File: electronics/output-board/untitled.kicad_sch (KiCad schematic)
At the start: 5 parts, among them J17 Conn_01x02_Male

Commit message: Started updating the output board
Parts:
- added D?: 1N4007, Diode_THT:D_DO-41_SOD81_P10.16mm_Horizontal, symbol Diode:1N4007
- renumbered D13 to D9, J17 to J12, MOSFET13 to MOSFET8, R30 to R10, R29 to R23
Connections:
- net +12V: now also D?.1 (K)
- net at D9.1 (K), J12.1 (Pin_1), MOSFET8.3: now also D?.2 (A)
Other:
- moved on the sheet: D9, J12, MOSFET8, R10, R23
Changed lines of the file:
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@@
 (kicad_sch (version 20211123) (generator eeschema)
   (paper "A4")
-  (junction (at 49.53 36.83) (diameter 0) (color 0 0 0 0)
+  (junction (at 49.53 43.18) (diameter 0) (color 0 0 0 0)
   )
-  (junction (at 46.99 30.48) (diameter 0) (color 0 0 0 0)
+  (junction (at 44.45 30.48) (diameter 0) (color 0 0 0 0)
   )
-  (wire (pts (xy 62.23 36.83) (xy 67.31 36.83))
+  (junction (at 46.99 36.83) (diameter 0) (color 0 0 0 0)
+  )
+  (junction (at 52.07 30.48) (diameter 0) (color 0 0 0 0)
+  )
+  (wire (pts (xy 62.23 43.18) (xy 67.31 43.18))
     (stroke (width 0) (type default) (color 0 0 0 0))
   )
-  (wire (pts (xy 46.99 30.48) (xy 58.42 30.48))
+  (wire (pts (xy 46.99 35.56) (xy 44.45 35.56))
     (stroke (width 0) (type default) (color 0 0 0 0))
   )
-  (wire (pts (xy 49.53 54.61) (xy 49.53 57.15))
+  (wire (pts (xy 49.53 35.56) (xy 52.07 35.56))
     (stroke (width 0) (type default) (color 0 0 0 0))
   )
-  (wire (pts (xy 49.53 36.83) (xy 54.61 36.83))
+  (wire (pts (xy 46.99 36.83) (xy 58.42 36.83))
     (stroke (width 0) (type default) (color 0 0 0 0))
   )
-  (wire (pts (xy 66.04 30.48) (xy 67.31 30.48))
+  (wire (pts (xy 52.07 22.86) (xy 52.07 30.48))
     (stroke (width 0) (type default) (color 0 0 0 0))
   )
-  (wire (pts (xy 67.31 30.48) (xy 67.31 36.83))
+  (wire (pts (xy 49.53 60.96) (xy 49.53 63.5))
     (stroke (width 0) (type default) (color 0 0 0 0))
   )
-  (wire (pts (xy 24.13 57.15) (xy 49.53 57.15))
+  (wire (pts (xy 49.53 43.18) (xy 54.61 43.18))
     (stroke (width 0) (type default) (color 0 0 0 0))
   )
-  (wire (pts (xy 49.53 29.21) (xy 49.53 36.83))
+  (wire (pts (xy 66.04 36.83) (xy 67.31 36.83))
     (stroke (width 0) (type default) (color 0 0 0 0))
   )
-  (wire (pts (xy 49.53 36.83) (xy 49.53 39.37))
+  (wire (pts (xy 67.31 36.83) (xy 67.31 43.18))
     (stroke (width 0) (type default) (color 0 0 0 0))
   )
-  (wire (pts (xy 34.29 46.99) (xy 39.37 46.99))
+  (wire (pts (xy 24.13 63.5) (xy 49.53 63.5))
     (stroke (width 0) (type default) (color 0 0 0 0))
   )
-  (wire (pts (xy 24.13 46.99) (xy 26.67 46.99))
+  (wire (pts (xy 49.53 35.56) (xy 49.53 43.18))
     (stroke (width 0) (type default) (color 0 0 0 0))
   )
-  (wire (pts (xy 46.99 29.21) (xy 46.99 30.48))
+  (wire (pts (xy 49.53 43.18) (xy 49.53 45.72))
     (stroke (width 0) (type default) (color 0 0 0 0))
   )
-  (wire (pts (xy 45.72 30.48) (xy 46.99 30.48))
+  (wire (pts (xy 52.07 35.56) (xy 52.07 30.48))
     (stroke (width 0) (type default) (color 0 0 0 0))
   )
-  (wire (pts (xy 45.72 33.02) (xy 45.72 30.48))
+  (wire (pts (xy 44.45 30.48) (xy 44.45 22.86))
     (stroke (width 0) (type default) (color 0 0 0 0))
   )
-  (hierarchical_label "GROUND" (shape input) (at 24.13 57.15 180)
+  (wire (pts (xy 44.45 35.56) (xy 44.45 30.48))
+    (stroke (width 0) (type default) (color 0 0 0 0))
+  )
+  (wire (pts (xy 34.29 53.34) (xy 39.37 53.34))
+    (stroke (width 0) (type default) (color 0 0 0 0))
+  )
+  (wire (pts (xy 24.13 53.34) (xy 26.67 53.34))
+    (stroke (width 0) (type default) (color 0 0 0 0))
+  )
+  (wire (pts (xy 46.99 35.56) (xy 46.99 36.83))
+    (stroke (width 0) (type default) (color 0 0 0 0))
+  )
+  (wire (pts (xy 45.72 36.83) (xy 46.99 36.83))
+    (stroke (width 0) (type default) (color 0 0 0 0))
+  )
+  (wire (pts (xy 45.72 39.37) (xy 45.72 36.83))
+    (stroke (width 0) (type default) (color 0 0 0 0))
+  )
+  (wire (pts (xy 44.45 22.86) (xy 46.99 22.86))
+    (stroke (width 0) (type default) (color 0 0 0 0))
+  )
+  (wire (pts (xy 49.53 22.86) (xy 52.07 22.86))
+    (stroke (width 0) (type default) (color 0 0 0 0))
+  )
+  (hierarchical_label "GROUND" (shape input) (at 24.13 63.5 180)
     (effects (font (size 1.27 1.27)) (justify right))
   )
-  (hierarchical_label "INPUT" (shape input) (at 24.13 46.99 180)
+  (hierarchical_label "INPUT" (shape input) (at 24.13 53.34 180)
     (effects (font (size 1.27 1.27)) (justify right))
   )
-  (symbol (lib_id "power:+12V") (at 45.72 33.02 180)
+  (symbol (lib_id "power:+12V") (at 45.72 39.37 180)
     (in_bom yes) (on_board yes) (fields_autoplaced)
-    (property "Reference" "#PWR0144" (id 0) (at 45.72 29.21 0)
+    (property "Reference" "#PWR0140" (id 0) (at 45.72 35.56 0)
       (effects (font (size 1.27 1.27)) hide)
     )
-    (property "Value" "+12V" (id 1) (at 45.72 37.5826 0))
-    (property "Footprint" "" (id 2) (at 45.72 33.02 0)
+    (property "Value" "+12V" (id 1) (at 45.72 43.9326 0))
+    (property "Footprint" "" (id 2) (at 45.72 39.37 0)
       (effects (font (size 1.27 1.27)) hide)
     )
-    (property "Datasheet" "" (id 3) (at 45.72 33.02 0)
+    (property "Datasheet" "" (id 3) (at 45.72 39.37 0)
       (effects (font (size 1.27 1.27)) hide)
     )
     (pin "1")
   )
-  (symbol (lib_id "2021-09-18_15-04-13:BSS806NEH6327XTSA1") (at 39.37 46.99 0)
+  (symbol (lib_id "2021-09-18_15-04-13:BSS806NEH6327XTSA1") (at 39.37 53.34 0)
     (in_bom yes) (on_board yes)
-    (property "Reference" "MOSFET13" (id 0) (at 55.3721 45.9253 0)
+    (property "Reference" "MOSFET8" (id 0) (at 55.3721 52.2753 0)
       (effects (font (size 1.524 1.524)) (justify left))
     )
-    (property "Value" "BSS806NEH6327XTSA1" (id 1) (at 35.0521 41.5843 0)
+    (property "Value" "BSS806NEH6327XTSA1" (id 1) (at 35.0521 47.9343 0)
       (effects (font (size 1.524 1.524)) (justify left))
     )
-    (property "Footprint" "MOSFET:BSS806NEH6327XTSA1" (id 2) (at 50.8 53.594 0)
+    (property "Footprint" "MOSFET:BSS806NEH6327XTSA1" (id 2) (at 50.8 59.944 0)
       (effects (font (size 1.524 1.524)) hide)
     )
-    (property "Datasheet" "" (id 3) (at 39.37 46.99 0)
+    (property "Datasheet" "" (id 3) (at 39.37 53.34 0)
       (effects (font (size 1.524 1.524)))
     )
@@
     (pin "3")
   )
-  (symbol (lib_id "Connector:Conn_01x02_Male") (at 49.53 24.13 270)
+  (symbol (lib_id "Connector:Conn_01x02_Male") (at 49.53 17.78 270)
     (in_bom yes) (on_board yes)
-    (property "Reference" "J17" (id 0) (at 50.5461 25.9139 90)
+    (property "Reference" "J12" (id 0) (at 50.5461 19.5639 90)
       (effects (font (size 1.27 1.27)) (justify left))
     )
-    (property "Value" "Conn_01x02_Male" (id 1) (at 41.6561 22.339 90)
+    (property "Value" "Conn_01x02_Male" (id 1) (at 41.6561 15.989 90)
       (effects (font (size 1.27 1.27)) (justify left))
     )
-    (property "Footprint" "CustomFootprints:LatchingConnector2POS" (id 2) (at 49.53 24.13 0)
+    (property "Footprint" "CustomFootprints:LatchingConnector2POS" (id 2) (at 49.53 17.78 0)
       (effects (font (size 1.27 1.27)) hide)
     )
-    (property "Datasheet" "~" (id 3) (at 49.53 24.13 0)
+    (property "Datasheet" "~" (id 3) (at 49.53 17.78 0)
       (effects (font (size 1.27 1.27)) hide)
     )
@@
     (pin "2")
   )
-  (symbol (lib_id "Device:R") (at 30.48 46.99 90)
+  (symbol (lib_id "Device:R") (at 30.48 53.34 90)
     (in_bom yes) (on_board yes) (fields_autoplaced)
-    (property "Reference" "R29" (id 0) (at 30.48 42.0074 90))
-    (property "Value" "1K" (id 1) (at 30.48 44.7825 90))
-    (property "Footprint" "Resistor_SMD:R_0603_1608Metric" (id 2) (at 30.48 48.768 90)
+    (property "Reference" "R23" (id 0) (at 30.48 48.3574 90))
+    (property "Value" "1K" (id 1) (at 30.48 51.1325 90))
+    (property "Footprint" "Resistor_SMD:R_0603_1608Metric" (id 2) (at 30.48 55.118 90)
       (effects (font (size 1.27 1.27)) hide)
     )
-    (property "Datasheet" "~" (id 3) (at 30.48 46.99 0)
+    (property "Datasheet" "~" (id 3) (at 30.48 53.34 0)
       (effects (font (size 1.27 1.27)) hide)
     )
@@
     (pin "2")
   )
-  (symbol (lib_id "Device:R") (at 62.23 30.48 90)
-    (in_bom yes) (on_board yes)
-    (property "Reference" "R30" (id 0) (at 62.23 28.0374 90))
-    (property "Value" "511" (id 1) (at 62.2775 30.5919 90))
-    (property "Footprint" "Resistor_SMD:R_0603_1608Metric" (id 2) (at 62.23 32.258 90)
+  (symbol (lib_id "Diode:1N4007") (at 48.26 30.48 0)
+    (in_bom yes) (on_board yes) (fields_autoplaced)
+    (property "Reference" "D?" (id 0) (at 48.26 25.2435 0))
+    (property "Value" "1N4007" (id 1) (at 48.26 28.0186 0))
+    (property "Footprint" "Diode_THT:D_DO-41_SOD81_P10.16mm_Horizontal" (id 2) (at 48.26 34.925 0)
       (effects (font (size 1.27 1.27)) hide)
     )
-    (property "Datasheet" "~" (id 3) (at 62.23 30.48 0)
+    (property "Datasheet" "http://www.vishay.com/docs/88503/1n4001.pdf" (id 3) (at 48.26 30.48 0)
       (effects (font (size 1.27 1.27)) hide)
     )
@@
     (pin "2")
   )
-  (symbol (lib_id "Device:LED") (at 58.42 36.83 0)
-    (in_bom yes) (on_board yes) (fields_autoplaced)
-    (property "Reference" "D13" (id 0) (at 58.2295 31.5934 0))
-    (property "Value" "LED" (id 1) (at 58.2295 34.3685 0))
-    (property "Footprint" "LED_SMD:LED_1206_3216Metric" (id 2) (at 58.42 36.83 0)
+  (symbol (lib_id "Device:R") (at 62.23 36.83 90)
+    (in_bom yes) (on_board yes)
+    (property "Reference" "R10" (id 0) (at 62.23 34.3874 90))
+    (property "Value" "511" (id 1) (at 62.2775 36.9419 90))
+    (property "Footprint" "Resistor_SMD:R_0603_1608Metric" (id 2) (at 62.23 38.608 90)
       (effects (font (size 1.27 1.27)) hide)
     )
-    (property "Datasheet" "~" (id 3) (at 58.42 36.83 0)
+    (property "Datasheet" "~" (id 3) (at 62.23 36.83 0)
       (effects (font (size 1.27 1.27)) hide)
     )
+    (pin "1")
+    (pin "2")
+  )
+  (symbol (lib_id "Device:LED") (at 58.42 43.18 0)
+    (in_bom yes) (on_board yes) (fields_autoplaced)
+    (property "Reference" "D9" (id 0) (at 58.2295 37.9434 0))
+    (property "Value" "LED" (id 1) (at 58.2295 40.7185 0))
+    (property "Footprint" "LED_SMD:LED_1206_3216Metric" (id 2) (at 58.42 43.18 0)
+      (effects (font (size 1.27 1.27)) hide)
+    )
+    (property "Datasheet" "~" (id 3) (at 58.42 43.18 0)
+      (effects (font (size 1.27 1.27)) hide)
+    )

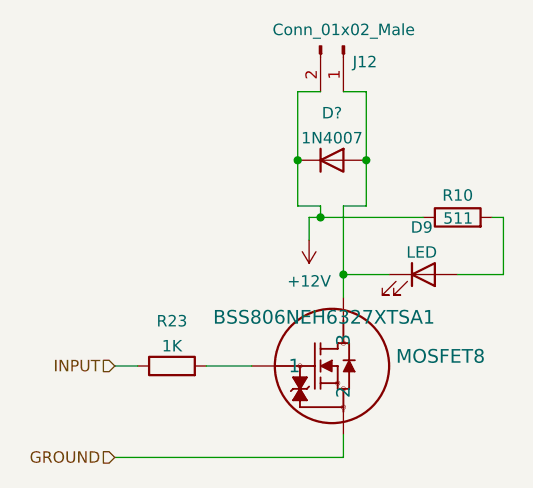
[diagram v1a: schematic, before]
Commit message: Revising Output Board
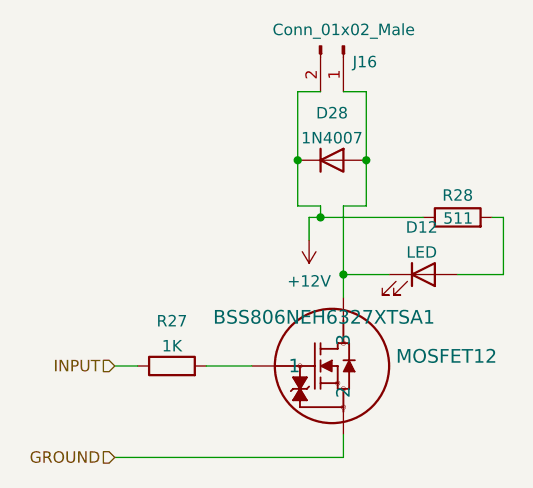
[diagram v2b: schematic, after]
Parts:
- D28: renamed from D?; footprint Diode_THT:D_DO-41_SOD81_P10.16mm_Horizontal -> Diode_SMD:D_1206_3216Metric
- renumbered D9 to D12, J12 to J16, MOSFET8 to MOSFET12, R23 to R27, R10 to R28
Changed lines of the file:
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@@
   (symbol (lib_id "power:+12V") (at 45.72 39.37 180)
     (in_bom yes) (on_board yes) (fields_autoplaced)
-    (property "Reference" "#PWR0140" (id 0) (at 45.72 35.56 0)
+    (property "Reference" "#PWR0143" (id 0) (at 45.72 35.56 0)
       (effects (font (size 1.27 1.27)) hide)
     )
@@
   (symbol (lib_id "2021-09-18_15-04-13:BSS806NEH6327XTSA1") (at 39.37 53.34 0)
     (in_bom yes) (on_board yes)
-    (property "Reference" "MOSFET8" (id 0) (at 55.3721 52.2753 0)
+    (property "Reference" "MOSFET12" (id 0) (at 55.3721 52.2753 0)
       (effects (font (size 1.524 1.524)) (justify left))
     )
@@
   (symbol (lib_id "Connector:Conn_01x02_Male") (at 49.53 17.78 270)
     (in_bom yes) (on_board yes)
-    (property "Reference" "J12" (id 0) (at 50.5461 19.5639 90)
+    (property "Reference" "J16" (id 0) (at 50.5461 19.5639 90)
       (effects (font (size 1.27 1.27)) (justify left))
     )
@@
   (symbol (lib_id "Device:R") (at 30.48 53.34 90)
     (in_bom yes) (on_board yes) (fields_autoplaced)
-    (property "Reference" "R23" (id 0) (at 30.48 48.3574 90))
+    (property "Reference" "R27" (id 0) (at 30.48 48.3574 90))
     (property "Value" "1K" (id 1) (at 30.48 51.1325 90))
     (property "Footprint" "Resistor_SMD:R_0603_1608Metric" (id 2) (at 30.48 55.118 90)
@@
   (symbol (lib_id "Diode:1N4007") (at 48.26 30.48 0)
     (in_bom yes) (on_board yes) (fields_autoplaced)
-    (property "Reference" "D?" (id 0) (at 48.26 25.2435 0))
+    (property "Reference" "D28" (id 0) (at 48.26 25.2435 0))
     (property "Value" "1N4007" (id 1) (at 48.26 28.0186 0))
-    (property "Footprint" "Diode_THT:D_DO-41_SOD81_P10.16mm_Horizontal" (id 2) (at 48.26 34.925 0)
+    (property "Footprint" "Diode_SMD:D_1206_3216Metric" (id 2) (at 48.26 34.925 0)
       (effects (font (size 1.27 1.27)) hide)
     )
@@
   (symbol (lib_id "Device:R") (at 62.23 36.83 90)
     (in_bom yes) (on_board yes)
-    (property "Reference" "R10" (id 0) (at 62.23 34.3874 90))
+    (property "Reference" "R28" (id 0) (at 62.23 34.3874 90))
     (property "Value" "511" (id 1) (at 62.2775 36.9419 90))
     (property "Footprint" "Resistor_SMD:R_0603_1608Metric" (id 2) (at 62.23 38.608 90)
@@
   (symbol (lib_id "Device:LED") (at 58.42 43.18 0)
     (in_bom yes) (on_board yes) (fields_autoplaced)
-    (property "Reference" "D9" (id 0) (at 58.2295 37.9434 0))
+    (property "Reference" "D12" (id 0) (at 58.2295 37.9434 0))
     (property "Value" "LED" (id 1) (at 58.2295 40.7185 0))
     (property "Footprint" "LED_SMD:LED_1206_3216Metric" (id 2) (at 58.42 43.18 0)
